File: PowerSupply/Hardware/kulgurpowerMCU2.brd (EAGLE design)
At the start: 102 x 57 mm, 80 parts, among them IC1 TPS77050, IC2 TPS77333DGK, X1 12Mhz, X6 C-GRID-10-70543, X7 C-GRID-10-70543, X8 C-GRID-10-70543, X9 C-GRID-10-70543

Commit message: Lot of changes to schematics. A lot.
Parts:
- removed AN3, BUZZER: TPB1,27, testpad:B1,27
- removed C51, C56: 0,1, SparkFun:0603-CAP
- removed CN1: (no value), adafruit:USB-MINIB
- removed D1, D3, D4, D5, D6: BAT54, diode:SOT23
- removed ERROR, HEARTBEAT: (no value), SparkFun:LED-0603
- removed IC1: TPS77050, texas:SOT23-DBV
- removed JP1: (no value), pinhead:2X07
- removed R47, R52: 1k, SparkFun:0603-RES
- removed R50: 100k, SparkFun:0603-RES
- removed R51: 18k, SparkFun:0603-RES
- removed S3: (no value), switch-omron:B3F-10XX
- removed S4, S5: SWITCH-MOMENTARY-212MM, SparkFun-Electromechanical:TACTILE-PTH-12MM
- removed SG2: BUZZERSMD3, SparkFun:BUZZER-CMT1102
- removed X6, X7, X8, X9: C-GRID-10-70543, con-molex:70543-10
- added AN0, EMLE, TP2, TP6, TP7: TPB1,27, testpad:B1,27
- added C12: 0.1, SparkFun:0603-CAP
- added C14: 0,1, SparkFun:0603-CAP
- added C16, C18, C41: (no value), rcl:C/6032-28R
- added C19, C21, C24: 100n, rcl:C0603
- added C20, C25: 2.2nF / 50V, smd-ipc:C0402
- added C23: 1uF/ 26V, resistor:C0805
- added C27, C30, C31, C32, C33, C34, C35, C36, C37, C38, C39: 0.1, rcl:C0603
- added CN2: (no value), adafruit:USB-MINIB
- added D7: BAT54, diode:SOT23
- added D8: LED-RGB-CC-THRUDIFFUSE, SparkFun-LED:LED-RGB-THRU
- added ERROR1, HEARTBEAT1, LED0, LED1, LED2, LED3, LED4, LED5, LED6, LED7: (no value), SparkFun:LED-0603
- added IC3: REG1117-5, burr-brown:SOT223
- added JP2: (no value), pinhead:2X07
- added L1: 4,7uH, wuerth-elektronik:WE-KI_0805_B
- added L2, L4, L5: 4,7uH, inductors:DR73
- added R20, R21, R28, R29, R30, R31, R32, R33, R34: 1k, rcl:R0603
- added R22: 47k, rcl:R0603
- added R23: 100k, rcl:R0603
- added R24, R25: 22r, rcl:R0603
- added R26: 30k, rcl:R0603
- added R27: 17k, rcl:R0603
- added S6: SW1, SparkFun-Electromechanical:TACTILE_SWITCH_SMD
- added S7: SW2, SparkFun-Electromechanical:TACTILE_SWITCH_SMD
- added S8: SW3, SparkFun-Electromechanical:TACTILE_SWITCH_SMD
- added S9: RESET, SparkFun-Electromechanical:TACTILE-PTH-SIDEEZ
- added SG1: BUZZERSMD3, SparkFun:BUZZER-CMT1102
- added SV2: (no value), con-lstb:MA13-2
- added TP10, TP15, TP5, TP8: TPB2,54, testpad:B2,54
- added TPLED0, TPLED1, TPLED2, TPLED3, TPLED4, TPLED5, TPLED6, TPLED7: LED0, testpad:B1,27
- added U$16, U$17, U$18, U$19: CSD97374Q4M, CSD97374Q4M:CSD97374Q4M
- added U$3: ER-OLEDM032-1, oled:ER-OLEDM032-1
- added U1, U2: MPU-6000QFN-24, SparkFun-Sensors:QFN-24-TESTING
- C13: value 0.1 -> 0,1
- C26: value 1uF/6V -> 100n; device resistor:C0603 -> rcl:C0603
- C29: value 47uF/16V -> 0.1; device rcl:C/6032-28R -> rcl:C0603
- L3: device wuerth-elektronik:WE-KI_0805_B -> inductors:DR73
- R10, R15, R19, R5, R6, R9: device SparkFun:0603-RES -> rcl:R0603
- R12: value 30k -> 1k; device SparkFun:0603-RES -> rcl:R0603
- R14: value 17k -> 1k; device SparkFun:0603-RES -> rcl:R0603
- R18: value 47k -> 680k; device SparkFun:0603-RES -> rcl:R0603
- R7, R8: value 22r -> 1k; device SparkFun:0603-RES -> rcl:R0603
- S1: value SWS001 -> PROG; device smd-special:SMS-001 -> SparkFun-Electromechanical:TACTILE-PTH-SIDEEZ
- S2: value SWITCH-MOMENTARY-212MM -> SW4; device SparkFun-Electromechanical:TACTILE-PTH-12MM -> SparkFun-Electromechanical:TACTILE_SWITCH_SMD
- TP1, TP3, TP4: value TPB2,54 -> TPB1,27; device testpad:B2,54 -> testpad:B1,27
- U$1: value ER-OLEDM032-1 -> EDLRD224V3R6C; device oled:ER-OLEDM032-1 -> supercap-EDLRD224V3R6C:EDLRD224V3R6C
- U$2: value EDLRD224V3R6C -> USB+SHIELD; device supercap-EDLRD224V3R6C:EDLRD224V3R6C -> SparkFun-Connectors:USB-B-PTH
- moved R8 75.1 mm to (76.0, 52.5), turned to 270 degrees
- moved R7 74.7 mm to (74.0, 52.5), turned to 270 degrees
- moved TP3 70.5 mm to (74.0, 55.5)
- moved L3 54.1 mm to (19.5, 38.0)
- moved R14 41.0 mm to (80.0, 52.5), turned to 270 degrees
- moved R18 40.7 mm to (53.9, 34.4), turned to 270 degrees
- moved C26 39.7 mm to (53.1, 20.5), flipped to the bottom
- moved S1 38.0 mm to (45.5, 2.00), turned to 0 degrees
- moved D2 37.8 mm to (46.8, 42.2), turned to 0 degrees
- moved R12 37.2 mm to (78.0, 52.5), turned to 270 degrees
- moved C3 35.4 mm to (66.1, 18.3), turned to 270 degrees
- moved VBAT0 34.8 mm to (14.9, 35.6), turned to 180 degrees
- moved C5 34.5 mm to (64.0, 18.3), turned to 270 degrees
- moved R9 34.3 mm to (67.4, 42.8), turned to 0 degrees
- moved R17 33.2 mm to (42.1, 17.4), turned to 270 degrees
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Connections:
- removed net !SS1: JP1.9, U$14.19
- removed net !SS12: U$14.75
- removed net !SS3: JP1.5, U$14.22
- removed net !SS5: U$14.64
- removed net !SS9: U$14.56
- removed net +5V: C28.1, D2.C, IC2.5, IC2.6
- removed net 19V: 19V.TP, R50.1
- removed net AN3: AN3.TP, C13.1, R50.2, R51.2, U$14.73
- removed net EN_PANDA: R47.1, SG2.1
- removed net N$32: U$14.71
- removed net N$33: U$14.70
- removed net N$34: U$14.65
- removed net N$35: U$14.63
- removed net N$43: JP1.6
- removed net SCK0: U$14.26
- removed net SCK1: JP1.1, U$14.21
- removed net SCK12: U$14.78
- removed net SCK3: U$14.24
- removed net SCK5: U$14.69
- removed net SCK6: U$14.16
- removed net SCK9: U$14.55
- removed net SCL0: U$14.34
- removed net SCL5: U$14.67
- removed net SDA0: U$14.33
- removed net SMISO0: U$14.27
- removed net SMISO1: JP1.11, U$14.20
- removed net SMISO12: U$14.76
- removed net SMISO3: U$14.23
- removed net SMISO5: U$14.68
- removed net SMISO6: U$14.17
- removed net SMISO9: U$14.54
- removed net SMOSI0: U$14.28
- removed net SMOSI12: U$14.77
- removed net SMOSI3: U$14.25
- removed net SMOSI5: U$14.66
- removed net SMOSI6: U$14.18
- removed net SMOSI9: U$14.53
- removed net VBATT: D1.3, TP3.TP, U$14.6, U$2.P
- new net !SKIP0: U$14.69, U$16.P$1
- new net !SKIP1: U$14.68, U$17.P$1
- new net !SKIP2: U$14.67, U$18.P$1
- new net !SKIP3: U$14.65, U$19.P$1
- new net !SW1: S6.3, S6.4, U$14.17
- new net !SW2: S7.3, S7.4, U$14.18
- new net !SW3!/TMS: JP2.9, S8.3, S8.4, U$14.19
- new net !SW4!/TDI: S2.3, S2.4, U$14.20
- new net !TRST: JP2.3, U$14.16
- new net +19V: 19V.TP, C30.1, C33.1, C36.1, C39.1, R23.2, SV2.14, SV2.16, U$16.P$5A, U$16.P$5B, U$16.P$5C, U$16.P$5D, U$16.P$5E, U$16.P$5F, U$17.P$5A, U$17.P$5B, U$17.P$5C, U$17.P$5D, U$17.P$5E, U$17.P$5F, U$18.P$5A, U$18.P$5B, U$18.P$5C, U$18.P$5D, U$18.P$5E, U$18.P$5F, U$19.P$5A, U$19.P$5B, U$19.P$5C, U$19.P$5D, U$19.P$5E, U$19.P$5F
- new net 5V: C16.+, C28.1, C29.1, C32.1, C35.1, C38.1, D2.C, IC2.5, IC2.6, IC3.2, U$16.P$2, U$17.P$2, U$18.P$2, U$19.P$2
- new net AN0: AN0.TP, C12.1, R18.1, R23.1, U$14.76
- new net BAT0_EN: SV2.9, U$14.59
- new net BAT1_EN: SV2.11, U$14.58
- new net BAT2_EN: SV2.13, U$14.57
- new net BAT3_EN: SV2.15, U$14.56
- new net CPOUT1: C20.1, U1.20
- new net CPOUT2: C25.1, U2.20
- new net CS: U$14.74, U1.8
- new net CS5: U$14.52, U2.8
- new net EN_PANDA1: R19.1, SG1.1
- new net INT_GYRO1: U$14.75, U1.12
- new net INT_GYRO2: U$14.48, U2.12
- new net LED0: LED0.A, TPLED0.TP, U$14.28
- new net LED1: LED1.A, TPLED1.TP, U$14.27
- new net LED2: LED2.A, TPLED2.TP, U$14.26
- new net LED3: LED3.A, TPLED3.TP, U$14.25
- new net LED4: LED4.A, TPLED4.TP, U$14.24
- new net LED5: LED5.A, TPLED5.TP, U$14.23
- new net LED6/TDO: JP2.5, LED6.A, TPLED6.TP, U$14.22
- new net LED7/TCK: JP2.1, JP2.11, LED7.A, TPLED7.TP, U$14.21
- new net LED_BLUE: R34.2, U$14.33
- new net LED_GREEN: R33.2, U$14.31
- new net LED_RED: R32.2, U$14.29
- new net MISO: U$14.71, U1.9
- new net MISO5: U$14.50, U2.9
- new net MOSI: U$14.72, U1.24
- new net MOSI5: U$14.49, U2.24
- new net N$10: LED3.C, R14.2
- new net N$11: LED4.C, R28.2
- new net N$12: LED5.C, R29.2
- new net N$13: LED6.C, R30.2
- new net N$14: LED7.C, R31.2
- new net N$15: D8.3, R33.1
- new net N$18: C37.1, U$19.P$7
- new net N$20: C37.2, U$19.P$6
- new net N$22: C27.1, U$16.P$7
- new net N$23: C27.2, U$16.P$6
- new net N$24: C34.1, U$18.P$7
- new net N$25: C34.2, U$18.P$6
- new net N$26: TP1.TP, U$14.39
- new net N$28: TP3.TP, U$14.41
- new net N$30: TP6.TP, U$14.63
- new net N$7: ERROR1.C, R21.2
- new net OUT1_EN: SV2.18, U$14.55
- new net OUT2_EN: SV2.20, U$14.54
- new net OUT3_EN: SV2.22, U$14.53
- new net OUT4_EN: SV2.24, U$14.78
- new net OUT5_EN: SV2.26, U$14.77
- new net PWM0: U$14.70, U$16.P$8
- new net PWM1: U$14.66, U$17.P$8
- new net PWM2: U$14.64, U$18.P$8
- new net PWM3: U$14.61, U$19.P$8
- new net REGOUT1: C19.1, U1.10
- new net REGOUT2: C24.1, U2.10
- new net SCLK: U$14.73, U1.23
- new net SCLK5: U$14.51, U2.23
- new net SUPERCAP: D7.3, U$1.P, U$14.6
- new net USB0_VBUS: R26.1, R27.2, U$14.30
- new net V+: C23.1, C41.+, IC3.3, SV2.12
- new net VSW0: L2.1, TP8.TP, U$16.P$4A, U$16.P$4B, U$16.P$4C, U$16.P$4D, U$16.P$4E, U$16.P$4F
- new net VSW1: L3.1, TP5.TP, U$17.P$4A, U$17.P$4B, U$17.P$4C, U$17.P$4D, U$17.P$4E, U$17.P$4F
- new net VSW2: L4.1, TP10.TP, U$18.P$4A, U$18.P$4B, U$18.P$4C, U$18.P$4D, U$18.P$4E, U$18.P$4F
- new net VSW3: L5.1, TP15.TP, U$19.P$4A, U$19.P$4B, U$19.P$4C, U$19.P$4D, U$19.P$4E, U$19.P$4F
- net !OLED_CS: now also JP2.10, U$3.P$16; no longer JP1.10, U$1.P$16
- net !OLED_DC: now also U$3.P$14; no longer U$1.P$14
- net !OLED_RD: now also U$3.P$12; no longer U$1.P$12
- net !OLED_RESET: now also U$3.P$15; no longer U$1.P$15
- net !OLED_WR: now also U$3.P$13; no longer U$1.P$13
- net !RESET: now also JP2.13, R22.2, S9.1; no longer JP1.13, R18.2, S3.3, S3.4
- net +3V3: now also C14.1, C18.+, C21.1, D7.1, JP2.8, L1.1, R22.1, U$3.P$2, U1.13, U2.13; no longer C29.+, C56.1, D1.1, JP1.8, L3.1, R18.1, U$1.P$2
- net AVCC0: now also C13.1, L1.2; no longer C51.1, L3.2
- net BUZZER: now also R19.2, U$14.100; no longer BUZZER.TP, R47.2
- net D+: now also CN2.D+, R25.2, U$2.D+; no longer CN1.D+, R8.2
- net D-: now also CN2.D-, R24.2, U$2.D-; no longer CN1.D-, R7.2
- net D0: now also U$3.P$4; no longer U$1.P$4
- net D1: now also U$3.P$5; no longer U$1.P$5
- net D2: now also U$3.P$6; no longer U$1.P$6
- net D3: now also U$3.P$7; no longer U$1.P$7
- net D4: now also U$3.P$8; no longer U$1.P$8
- net D5: now also U$3.P$9; no longer U$1.P$9
- net D6: now also U$3.P$10; no longer U$1.P$10
- net D7: now also U$3.P$11; no longer U$1.P$11
- net EMLE: now also EMLE.TP, JP2.4; no longer JP1.4, TP1.TP
- net ERROR: now also ERROR1.A; no longer ERROR.A
- net GND: now also C12.2, C14.2, C16.-, C18.-, C19.2, C20.2, C21.2, C23.2, C24.2, C25.2, C29.2, C30.2, C32.2, C33.2, C35.2, C36.2, C38.2, C39.2, C41.-, CN2.GND, D8.2, IC3.1, JP2.12, JP2.14, JP2.2, R12.1, R14.1, R18.2, R20.1, R21.1, R26.2, R28.1, R29.1, R30.1, R31.1, R7.1, R8.1, S1.2, S2.1, S2.2, S6.1, S6.2, S7.1, S7.2, S8.1, S8.2, S9.2, SG1.2, SV2.10, SV2.17, U$1.N, U$16.P$3, U$16.PAD@1, U$17.P$3, U$17.PAD@1, U$18.P$3, U$18.PAD@1, U$19.P$3, U$19.PAD@1, U$2.GND, U$2.S1, U$2.S2, U$3.P$1, U1.1, U1.18, U2.1, U2.18; no longer C29.-, C51.2, C56.2, CN1.GND, IC1.2, JP1.12, JP1.14, JP1.2, R12.2, R19.1, R51.1, R52.1, S1.1, S3.1, S3.2, SG2.2, U$1.P$1, U$2.N, X6.3, X7.3, X8.3, X9.3
- net HEARTBEAT: now also HEARTBEAT1.A, U$14.34; no longer HEARTBEAT.A, U$14.100
- net IBAT0_AD: now also SV2.19; no longer X6.2
- net IBAT1_AD: now also SV2.21; no longer X7.2
- net IBAT2_AD: now also SV2.23; no longer X8.2
- net IBAT3_AD: now also SV2.25; no longer X9.2
- net MD: now also JP2.7, S1.1; no longer JP1.7, S1.2, TP4.TP
- net N$17: now also D8.4, R34.1; no longer HEARTBEAT.C, R19.2
- net N$19: now also C31.1, U$17.P$7; no longer U$14.31
- net N$2: now also LED0.C, R7.2; no longer R12.1, R14.2, U$14.30
- net N$21: now also C31.2, U$17.P$6; no longer U$14.4
- net N$27: now also TP2.TP, U$14.40; no longer U$14.74
- net N$29: now also TP4.TP, U$14.4; no longer ERROR.C, R52.2
- net N$31: now also TP7.TP, U$14.47; no longer U$14.72
- net N$4: now also D8.1, R32.1; no longer D3.3, D4.3, D5.3, D6.3, IC1.1
- net N$5: now also HEARTBEAT1.C, R20.2; no longer IC1.3
- net N$8: now also LED1.C, R8.2; no longer IC1.5
- net N$9: now also LED2.C, R12.2; no longer IC1.4
- net USB0_DM: now also R24.1; no longer R7.1
- net USB0_DP: now also R25.1; no longer R8.1
- net VBAT0: now also L2.2, SV2.1, SV2.2; no longer D3.1, X6.1
- net VBAT1: now also L3.2, SV2.3, SV2.4; no longer D4.1, X7.1
- net VBAT2: now also L4.2, SV2.5, SV2.6; no longer D5.1, X8.1
- net VBAT3: now also L5.2, SV2.7, SV2.8; no longer D6.1, X9.1
- net VBUS: now also CN2.VBUS, R27.1, U$2.VBUS; no longer CN1.VBUS, R14.1
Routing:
- net GND: track 332.5 -> 498.2 mm
- net 5V: track 0.00 -> 132.4 mm
- net VBATT: track 94.3 -> 0.00 mm, vias 2 -> 0
- net +19V: track 0.00 -> 92.6 mm, vias 0 -> 1
- net !SW3!/TMS: track 0.00 -> 78.8 mm, vias 0 -> 1
- net AN3: track 70.8 -> 0.00 mm
- net SUPERCAP: track 0.00 -> 70.0 mm, vias 0 -> 1
- net LED7/TCK: track 0.00 -> 68.6 mm, vias 0 -> 1
- net +3V3: track 144.3 -> 210.6 mm
- net PWM0: track 0.00 -> 65.5 mm, vias 0 -> 2
- net !SKIP0: track 0.00 -> 63.7 mm, vias 0 -> 2
- net USB0_DP: track 77.0 -> 14.2 mm, vias 2 -> 0
- net IBAT1_AD: track 98.2 -> 35.9 mm
- net USB0_DM: track 75.4 -> 13.2 mm, vias 2 -> 0
- net PWM1: track 0.00 -> 59.8 mm, vias 0 -> 2
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
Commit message: lot of work done on schematics
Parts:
- removed SV2: (no value), con-lstb:MA13-2
- removed TP6, TP7: TPB1,27, testpad:B1,27
- added X2: 2534-, con-3m:PAK100/2500-34
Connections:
- removed net N$30: TP6.TP, U$14.63
- removed net N$31: TP7.TP, U$14.47
- new net COMPUTER_PWR: U$14.47, X2.28
- new net ENABLE_PWR: U$14.63, X2.30
- new net IMON1: X2.27
- new net IMON2: X2.29
- new net PGOOD1: X2.31
- new net PGOOD2: X2.33
- new net PWM_A: X2.34
- new net PWM_B: X2.32
- net +19V: now also X2.14, X2.16; no longer SV2.14, SV2.16
- net BAT0_EN: now also X2.9; no longer SV2.9
- net BAT1_EN: now also X2.11; no longer SV2.11
- net BAT2_EN: now also X2.13; no longer SV2.13
- net BAT3_EN: now also X2.15; no longer SV2.15
- net GND: now also X2.10, X2.17; no longer SV2.10, SV2.17
- net IBAT0_AD: now also X2.19; no longer SV2.19
- net IBAT1_AD: now also X2.21; no longer SV2.21
- net IBAT2_AD: now also X2.23; no longer SV2.23
- net IBAT3_AD: now also X2.25; no longer SV2.25
- net OUT1_EN: now also X2.18; no longer SV2.18
- net OUT2_EN: now also X2.20; no longer SV2.20
- net OUT3_EN: now also X2.22; no longer SV2.22
- net OUT4_EN: now also X2.24; no longer SV2.24
- net OUT5_EN: now also X2.26; no longer SV2.26
- net V+: now also X2.12; no longer SV2.12
- net VBAT0: now also X2.1, X2.2; no longer SV2.1, SV2.2
- net VBAT1: now also X2.3, X2.4; no longer SV2.3, SV2.4
- net VBAT2: now also X2.5, X2.6; no longer SV2.5, SV2.6
- net VBAT3: now also X2.7, X2.8; no longer SV2.7, SV2.8
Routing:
- net COMPUTER_PWR: track 0.00 -> 32.2 mm, vias 0 -> 1
- net ENABLE_PWR: track 0.00 -> 20.9 mm
- net VBAT2_AD: track 68.4 -> 55.7 mm
- net BAT2_EN: track 33.1 -> 44.7 mm
- net OUT1_EN: track 27.2 -> 38.3 mm
- net N$30: track 10.9 -> 0.00 mm
- net BAT1_EN: track 38.4 -> 49.2 mm
- net OUT4_EN: track 23.4 -> 34.0 mm, vias 1 -> 2
- net BAT0_EN: track 37.7 -> 48.1 mm
- net IBAT0_AD: track 39.0 -> 49.4 mm
- net IBAT3_AD: track 28.2 -> 38.4 mm
- net OUT2_EN: track 24.8 -> 35.1 mm
- net +19V: track 92.6 -> 102.7 mm
- net OUT3_EN: track 22.6 -> 32.7 mm
- net BAT3_EN: track 32.2 -> 42.1 mm
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
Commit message: More work on electronics
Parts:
- removed ERROR1, HEARTBEAT1: (no value), SparkFun:LED-0603
- removed R20, R21: 1k, rcl:R0603
- removed TP1, TP2, TP3, TP4: TPB1,27, testpad:B1,27
- added C22, C40: 0.1, rcl:C0603
- added C42, C43, C44, C45: (no value), rcl:C/6032-28R
- added C46, C47, C48, C49: 0,1, SparkFun:0603-CAP
- added R35, R36: 10k, rcl:R0603
- added X3: 22-23-2021, con-molex:22-23-2021
- moved CN2 18.0 mm to (48.0, 52.5)
- moved U$2 11.0 mm to (62.0, 48.0)
- moved R24 3.61 mm to (62.4, 42.3)
- moved R25 3.61 mm to (60.2, 42.2)
- moved IC3 1.23 mm to (12.9, 20.3)
- moved R10 1.00 mm to (73.9, 43.8)
- moved C34 0.98 mm to (26.8, 52.0)
- moved C31 0.95 mm to (17.9, 52.2)
- moved C37 0.93 mm to (35.9, 52.1)
- moved C27 0.86 mm to (8.83, 52.3)
- moved R9 0.78 mm to (67.4, 43.5)
- moved R19 0.57 mm to (79.4, 23.0)
- moved C30 0.45 mm to (31.0, 52.0)
- moved C33 0.33 mm to (40.0, 52.2)
- moved C16 0.31 mm to (10.9, 12.0)
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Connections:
- net CS renamed SSLB0
- net MISO renamed MISOB
- net MOSI renamed MOSIB
- net N$1 renamed USB0_DPUPE
- removed net CS5: U$14.52, U2.8
- removed net ERROR: ERROR1.A, U$14.98
- removed net HEARTBEAT: HEARTBEAT1.A, U$14.34
- removed net MISO5: U$14.50, U2.9
- removed net MOSI5: U$14.49, U2.24
- removed net N$26: TP1.TP, U$14.39
- removed net N$27: TP2.TP, U$14.40
- removed net N$28: TP3.TP, U$14.41
- removed net N$29: TP4.TP, U$14.4
- removed net N$5: HEARTBEAT1.C, R20.2
- removed net N$7: ERROR1.C, R21.2
- removed net PWM_A: X2.34
- removed net PWM_B: X2.32
- removed net SCLK: U$14.73, U1.23
- removed net SCLK5: U$14.51, U2.23
- new net AN1: C22.1, R35.2, U$14.75
- new net AN3: C40.1, R36.2, U$14.73
- new net MISOA: R9.2, U$14.45, U2.9
- new net MOSIA: U$14.46, U2.24
- new net PWM4: U$14.56, X2.34
- new net PWM5: U$14.54, X2.32
- new net RSPCKA: U$14.47, U2.23
- new net RSPCKB: U$14.77, U1.23
- new net SSLA0: U$14.48, U2.8
- net !OLED_CS: now also U$14.39; no longer U$14.46
- net !OLED_DC: now also U$14.40; no longer R9.2, U$14.45
- net !TRST: now also X3.1
- net +3V3: now also C46.1, C47.1, C48.1, C49.1
- net BAT0_EN: now also U$14.63; no longer U$14.59
- net BAT1_EN: now also U$14.59; no longer U$14.58
- net BAT2_EN: now also U$14.58; no longer U$14.57
- net BAT3_EN: now also U$14.57; no longer U$14.56
- net COMPUTER_PWR: now also U$14.78; no longer U$14.47
- net ENABLE_PWR: now also U$14.34; no longer U$14.63
- net GND: now also C22.2, C40.2, C42.-, C43.-, C44.-, C45.-, C46.2, C47.2, C48.2, C49.2, X3.2; no longer R20.1, R21.1
- net IMON1: now also R35.1
- net IMON2: now also R36.1
- net INT_GYRO1: now also U$14.51; no longer U$14.75
- net INT_GYRO2: now also U$14.52; no longer U$14.48
- net OUT2_EN: now also U$14.53; no longer U$14.54
- net OUT3_EN: now also U$14.4; no longer U$14.53
- net OUT4_EN: now also U$14.41; no longer U$14.78
- net OUT5_EN: now also U$14.98; no longer U$14.77
- net PGOOD1: now also U$14.49
- net PGOOD2: now also U$14.50
- net VBAT0: now also C42.+
- net VBAT1: now also C43.+
- net VBAT2: now also C44.+
- net VBAT3: now also C45.+
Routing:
- net GND: track 500.1 -> 569.6 mm, vias 4 -> 9
- net HEARTBEAT: track 33.9 -> 0.00 mm, vias 2 -> 0
- net MISOA: track 0.00 -> 32.1 mm, vias 0 -> 1
- net PGOOD1: track 0.00 -> 29.1 mm, vias 0 -> 1
- net SSLA0: track 0.00 -> 28.0 mm, vias 0 -> 1
- net MISO5: track 27.6 -> 0.00 mm, vias 1 -> 0
- net PGOOD2: track 0.00 -> 24.5 mm, vias 0 -> 1
- net CS5: track 23.9 -> 0.00 mm, vias 1 -> 0
- net RSPCKA: track 0.00 -> 22.7 mm, vias 0 -> 1
- net MOSIA: track 0.00 -> 22.1 mm, vias 0 -> 1
- net MOSI5: track 21.5 -> 0.00 mm, vias 1 -> 0
- net N$26: track 21.5 -> 0.00 mm, vias 2 -> 0
- net PWM5: track 0.00 -> 20.3 mm
- net OUT3_EN: track 32.7 -> 51.8 mm, vias 1 -> 2
- net N$27: track 18.8 -> 0.00 mm, vias 2 -> 0
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
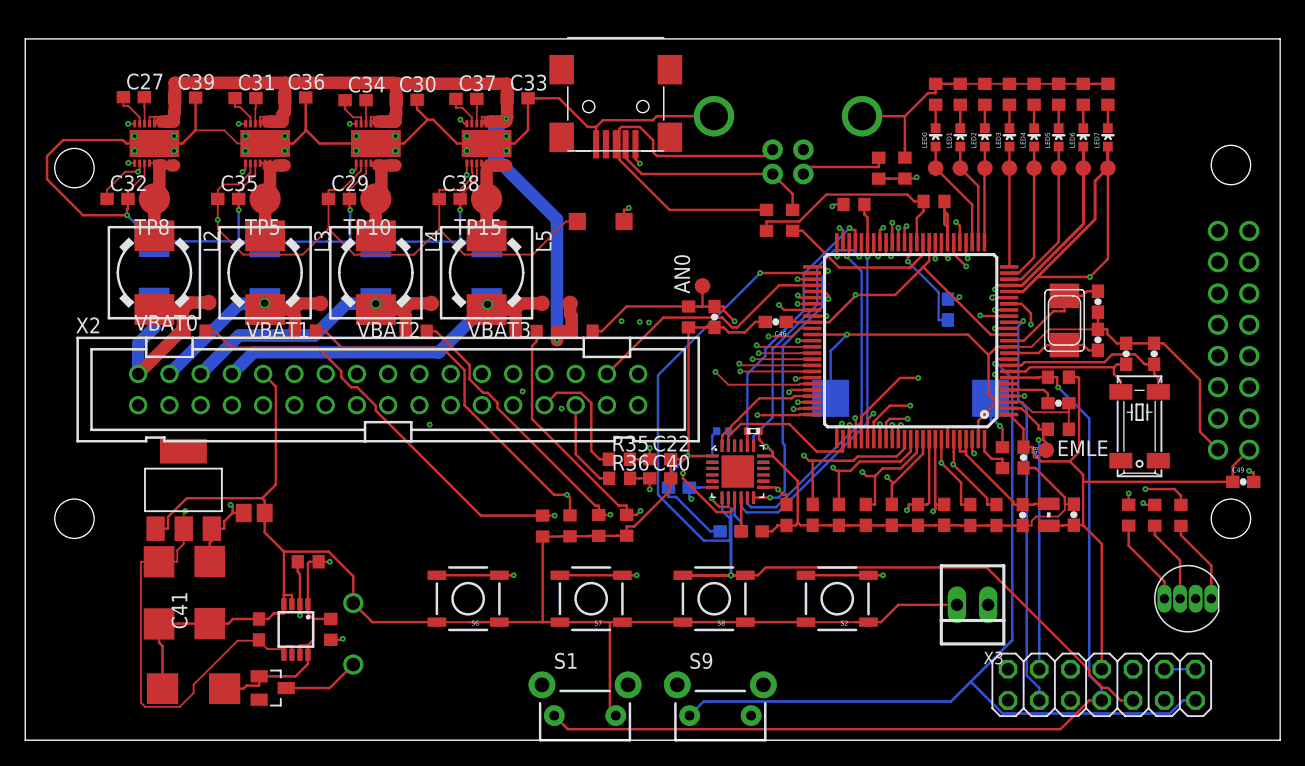
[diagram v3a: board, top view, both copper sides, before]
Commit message: Converted into 2 layer board from 4 layer. Seems to be OK for production
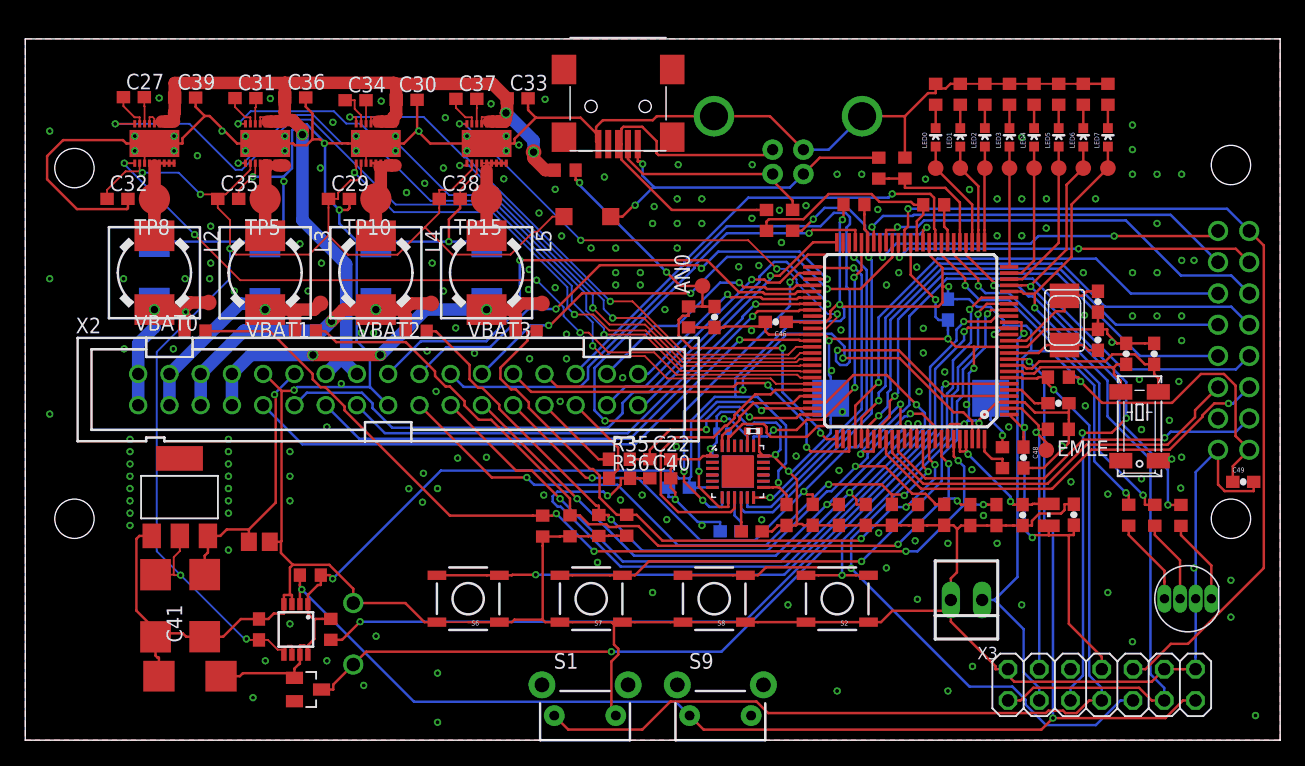
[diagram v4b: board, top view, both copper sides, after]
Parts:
- moved R23 13.2 mm to (43.9, 46.3)
- moved 19V 12.7 mm to (41.3, 47.8)
- moved D7 2.88 mm to (23.0, 4.12)
- moved C23 2.38 mm to (19.0, 16.1)
- moved D2 1.15 mm to (45.7, 42.6)
- moved C41 1.14 mm to (14.6, 10.9)
- moved R22 1.09 mm to (23.2, 13.4)
- moved C16 1.09 mm to (10.6, 10.9)
- moved C18 1.05 mm to (13.4, 5.20)
- moved IC3 0.67 mm to (12.5, 19.8)
- moved X3 0.64 mm to (76.5, 11.4)
- moved R10 0.28 mm to (73.8, 43.5)
- moved CN2 0.19 mm to (48.2, 52.5)
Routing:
- net AN3: track 18.6 -> 59.1 mm
- net LED7: track 31.5 -> 0.00 mm
- net LED6: track 28.8 -> 0.00 mm
- net RSPCKA: track 22.7 -> 44.6 mm, vias 1 -> 3
- net !SW3: track 21.1 -> 0.00 mm, vias 2 -> 0
- net OUT3_EN: track 51.8 -> 69.3 mm, vias 2 -> 1
- net GND: track 569.6 -> 553.7 mm, vias 9 -> 209
- net +19V: track 101.1 -> 87.3 mm, vias 2 -> 3
- net D4: track 34.1 -> 47.5 mm
- net 5V: track 128.3 -> 115.5 mm, vias 3 -> 5
- net AN0: track 28.8 -> 40.1 mm, vias 2 -> 4
- net +3V3: track 209.1 -> 198.2 mm, vias 6 -> 9
- net INT_GYRO2: track 36.8 -> 26.6 mm, vias 1 -> 3
- net N$1: track 9.70 -> 0.00 mm
- net D3: track 31.2 -> 40.7 mm
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- added copper zone on layer 1, net GND
- added copper zone on layer 16, net GND

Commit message: Silkscreen fixes
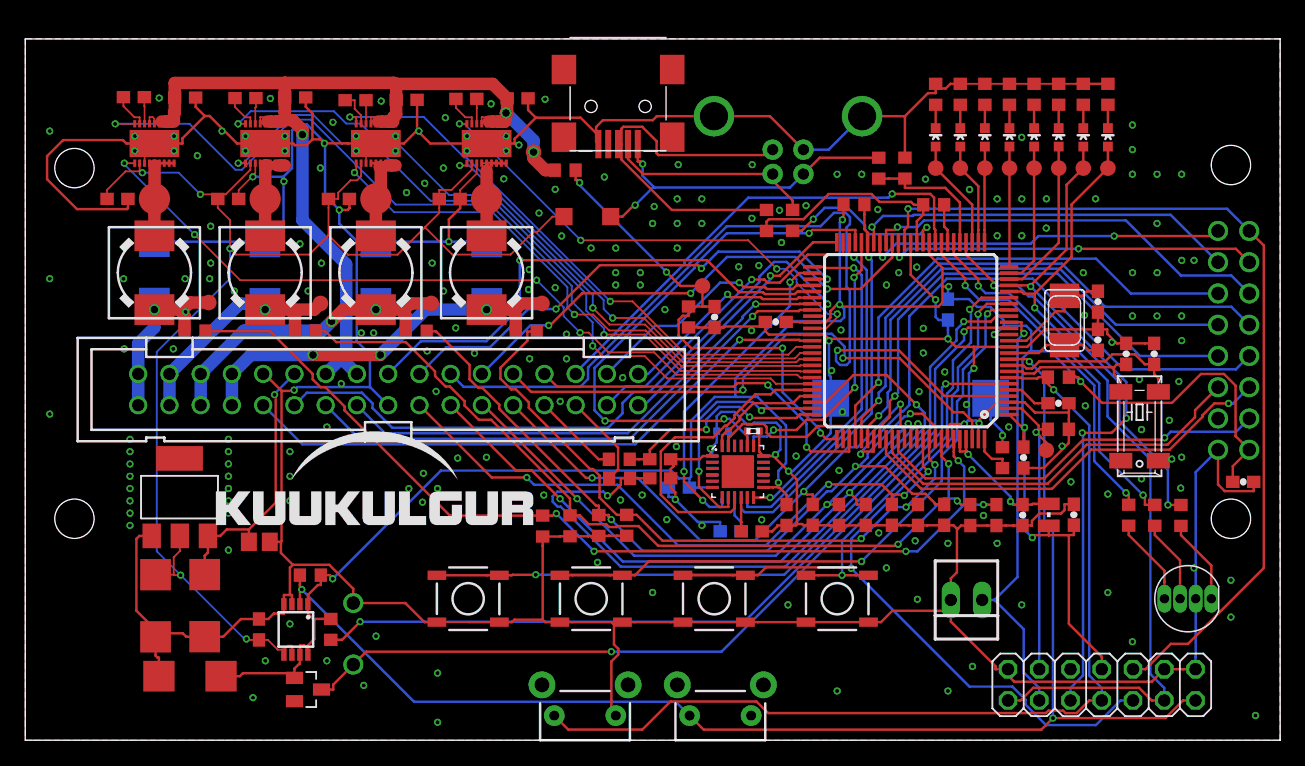
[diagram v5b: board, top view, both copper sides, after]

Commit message: Minor bugfixes to boards.
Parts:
- added D1: MBRS320T3, diode:SMC
- D8: value LED-RGB-CC-THRUDIFFUSE -> WP154A4SUREQBFZGW
- moved C18 0.75 mm to (13.4, 4.45)
- moved C31 0.25 mm to (17.7, 52.2)
- moved C37 0.25 mm to (35.6, 52.1)
- moved C36 0.06 mm to (21.9, 52.2)
- moved C27 0.06 mm to (8.83, 52.2)
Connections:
- net EN_PANDA1 renamed BUZZER_X
- new net VIN: C30.1, C33.1, C36.1, C39.1, D1.C, U$16.P$5A, U$16.P$5B, U$16.P$5C, U$16.P$5D, U$16.P$5E, U$16.P$5F, U$17.P$5A, U$17.P$5B, U$17.P$5C, U$17.P$5D, U$17.P$5E, U$17.P$5F, U$18.P$5A, U$18.P$5B, U$18.P$5C, U$18.P$5D, U$18.P$5E, U$18.P$5F, U$19.P$5A, U$19.P$5B, U$19.P$5C, U$19.P$5D, U$19.P$5E, U$19.P$5F
- net +19V: now also D1.A; no longer C30.1, C33.1, C36.1, C39.1, U$16.P$5A, U$16.P$5B, U$16.P$5C, U$16.P$5D, U$16.P$5E, U$16.P$5F, U$17.P$5A, U$17.P$5B, U$17.P$5C, U$17.P$5D, U$17.P$5E, U$17.P$5F, U$18.P$5A, U$18.P$5B, U$18.P$5C, U$18.P$5D, U$18.P$5E, U$18.P$5F, U$19.P$5A, U$19.P$5B, U$19.P$5C, U$19.P$5D, U$19.P$5E, U$19.P$5F
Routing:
- net VIN: track 0.00 -> 127.8 mm, vias 0 -> 12
- net +19V: track 87.3 -> 2.63 mm, vias 3 -> 4
- net GND: track 553.7 -> 553.8 mm, vias 209 -> 280
- added copper zone on layer 15, net +19V
- added copper zone on layer 15, net +3V3
- added copper zone on layer 2, net GND
- added copper zone on layer 15, net VIN

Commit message: Two resistors in ladder were swapped Nominals rised for pullup. Next power bill will be smaller!
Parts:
- R18: value 680k -> 100k
- R23: value 100k -> 680k
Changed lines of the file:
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@@
 <attribute name="TP_SIGNAL_NAME" value="" x="56.9517" y="36.2865" size="1" layer="37" rot="R90"/>
 </element>
-<element name="R18" library="rcl" package="R0603" value="680k" x="53.9152" y="34.4035" smashed="yes" rot="R270"/>
-<element name="R23" library="rcl" package="R0603" value="100k" x="43.8868" y="46.3333" smashed="yes" rot="R180"/>
+<element name="R18" library="rcl" package="R0603" value="100k" x="53.9152" y="34.4035" smashed="yes" rot="R270"/>
+<element name="R23" library="rcl" package="R0603" value="680k" x="43.8868" y="46.3333" smashed="yes" rot="R180"/>
 <element name="R24" library="rcl" package="R0603" value="22r" x="62.3747" y="42.2561" smashed="yes" rot="R90"/>
 <element name="R25" library="rcl" package="R0603" value="22r" x="60.2494" y="42.2491" smashed="yes" rot="R90"/>
